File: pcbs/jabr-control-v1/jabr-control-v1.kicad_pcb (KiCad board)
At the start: 6 copper layers, 71 x 43 mm, 7 parts, among them J4001 MDT275E01001, J8001 MSPE-J2L0-x00, U3001 PI7C9X2G303EL, U5001 LAN7431_YXX, U6001 LAN8870, U7001 STM32H533CEUx

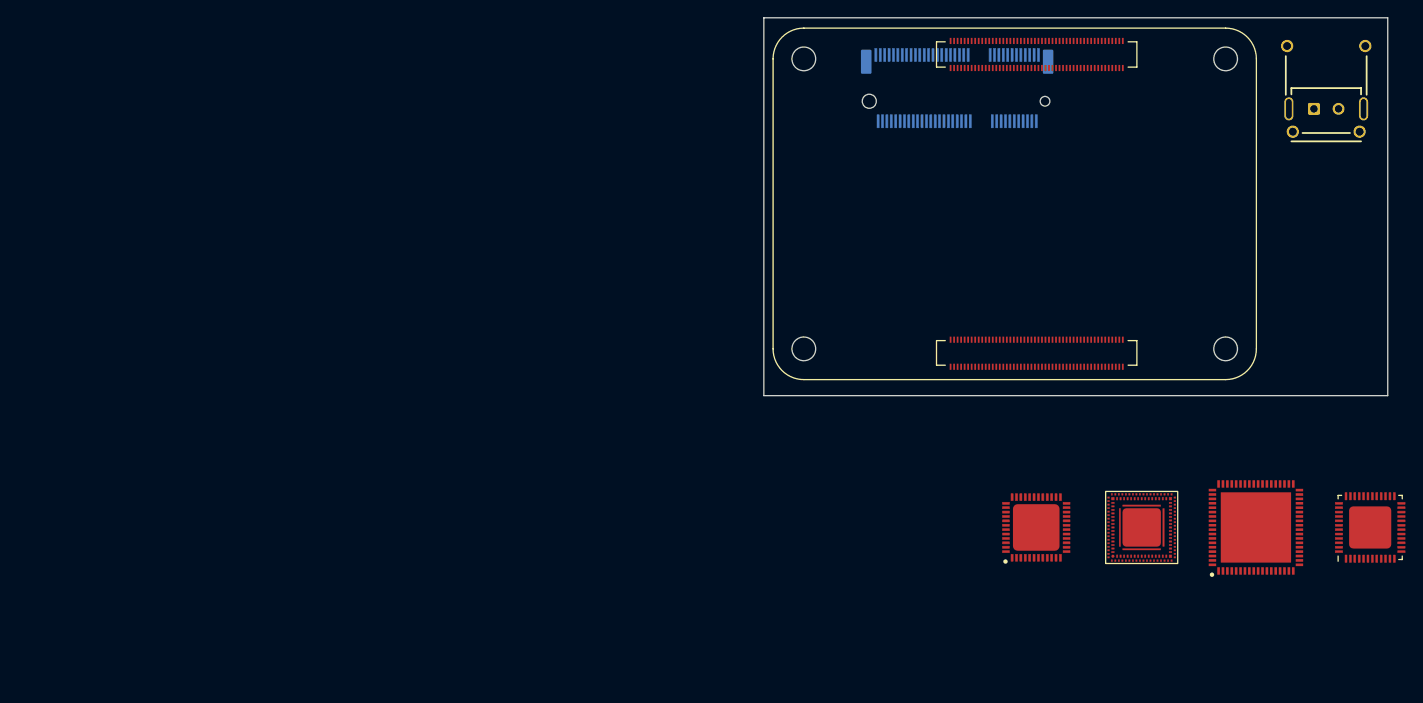
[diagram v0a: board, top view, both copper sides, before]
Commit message: Added PCIe connections
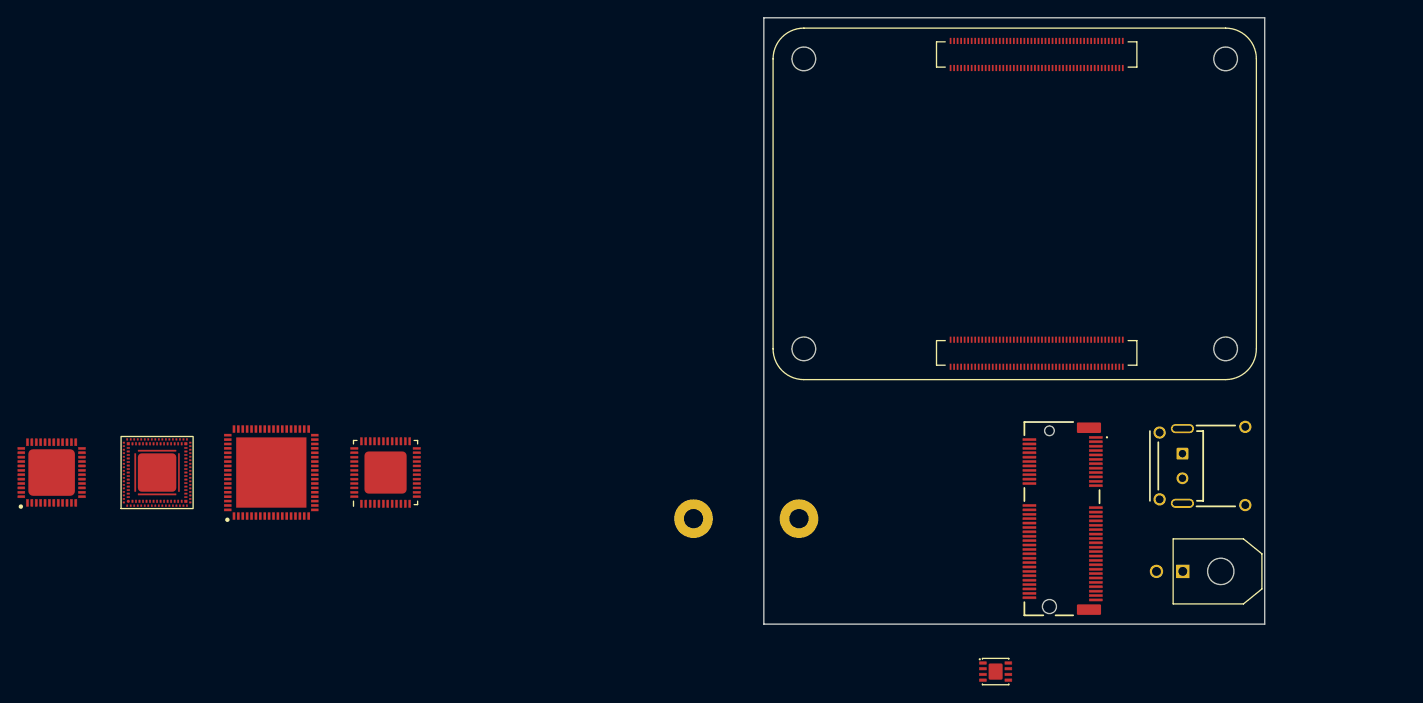
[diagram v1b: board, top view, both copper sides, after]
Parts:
- added H4001: MountingHole_Pad, MountingHole:MountingHole_2.2mm_M2_Pad, F.Cu at (125.0, 134.0)
- added H4002: MountingHole_Pad, MountingHole:MountingHole_2.2mm_M2_Pad, F.Cu at (113.0, 134.0)
- added J9001: 43045-0201, project_footprints:43045-02YY, F.Cu at (168.7, 140.0)
- added U9001: TVS3301DRBR, project_footprints:SON65P300X300X100-9N-D, F.Cu at (147.4, 151.4)
- J4001: moved to F.Cu
- moved U3001 112.2 mm to (52.0, 128.8)
- moved U5001 112.2 mm to (65.0, 128.8)
- moved U6001 112.2 mm to (78.0, 128.8)
- moved U7001 112.2 mm to (40.0, 128.8)
- moved J4001 50.4 mm to (155.0, 134.0), turned to -90 degrees
- moved J8001 43.8 mm to (168.6, 128.0), turned to 90 degrees
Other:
- board size 71 x 43 mm -> 57 x 69 mm

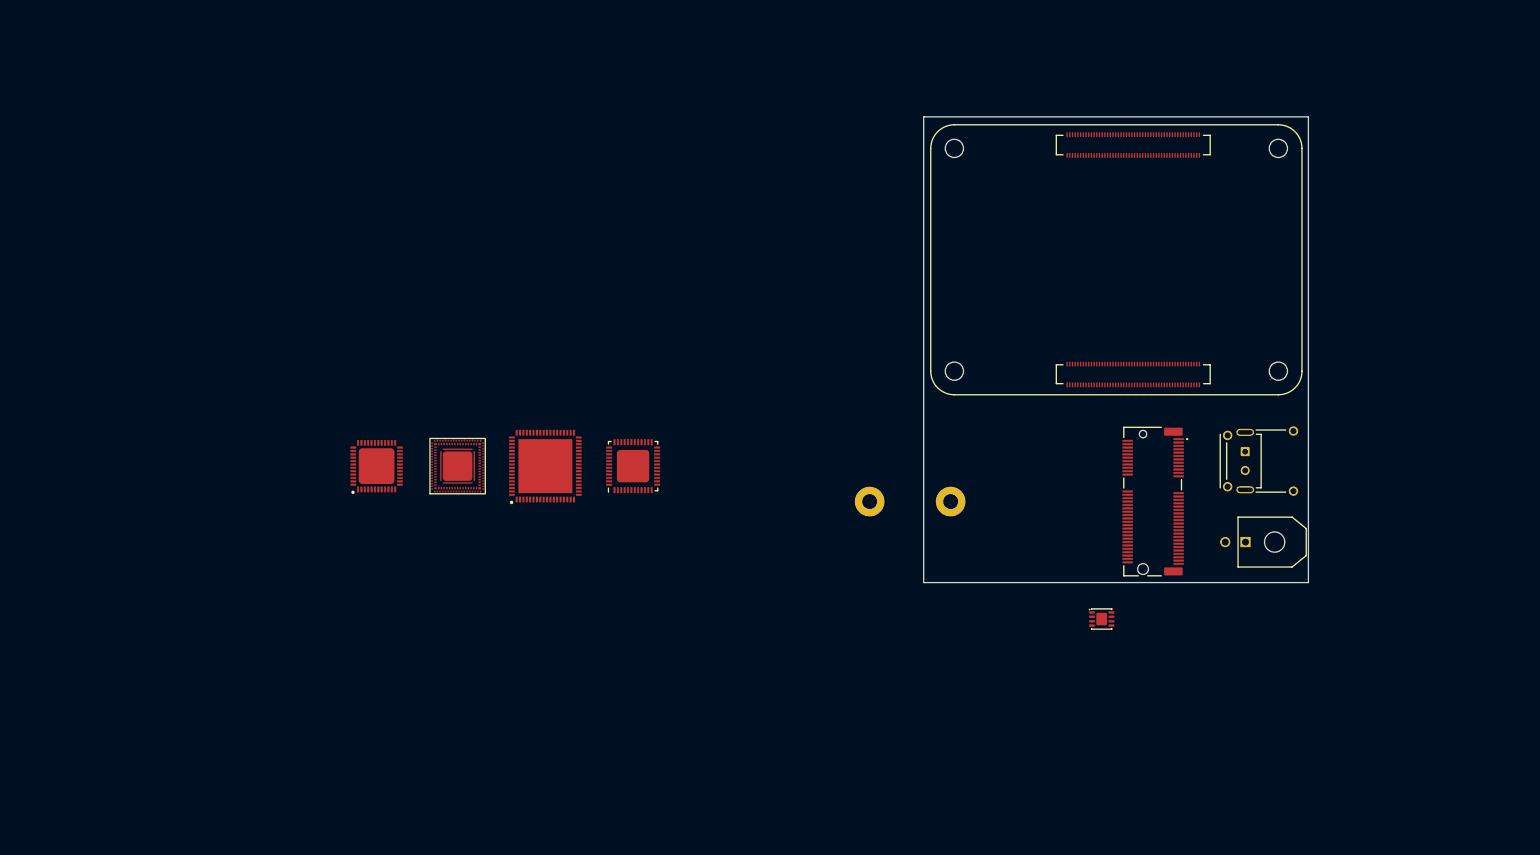
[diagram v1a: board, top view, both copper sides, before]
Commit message: Added power sheets
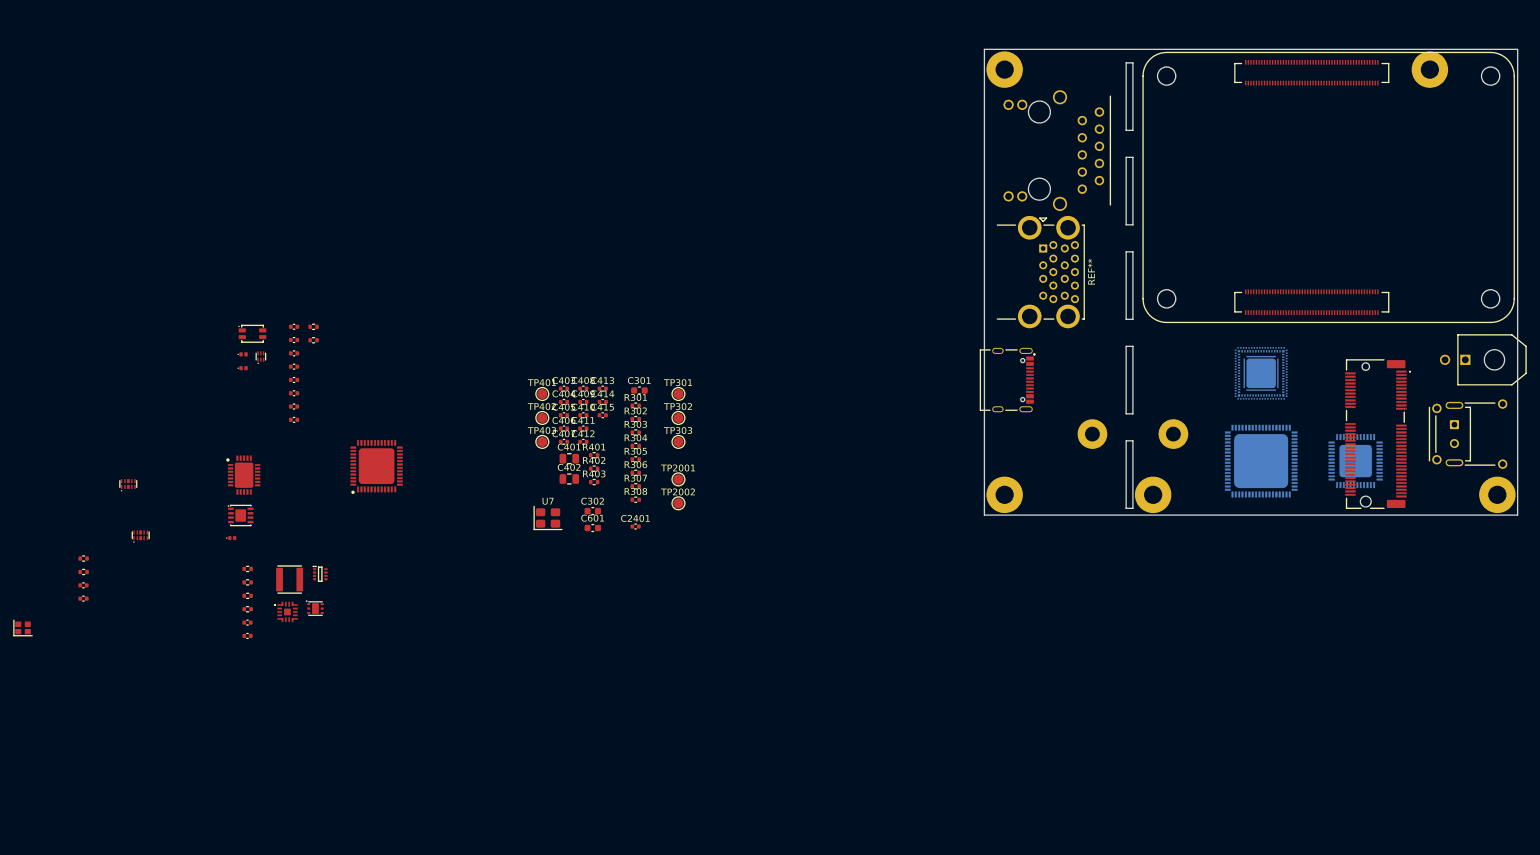
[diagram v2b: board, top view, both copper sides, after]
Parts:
- removed J8001: MSPE-J2L0-x00, project_footprints:MSPEJ2L0x00
- removed U6001: LAN8870, project_footprints:lan8870
- removed U9001: TVS3301DRBR, project_footprints:SON65P300X300X100-9N-D
- added C2401: 100n, Capacitor_SMD:C_0402_1005Metric, F.Cu at (78.3, 137.7)
- added C2935: 10p, project_footprints:C_0402, F.Cu at (-3.48, 146.4)
- added C2936: 10p, project_footprints:C_0402, F.Cu at (-3.48, 148.4)
- added C3001: 220n, project_footprints:C_0402, F.Cu at (27.7, 108.1)
- added C3002: 220n, project_footprints:C_0402, F.Cu at (27.7, 110.1)
- added C3003: 100n, project_footprints:C_0402, F.Cu at (27.7, 112.0)
- added C3004: 100n, project_footprints:C_0402, F.Cu at (27.7, 114.0)
- added C3005: 220n, project_footprints:C_0402, F.Cu at (27.7, 116.0)
- added C3006: 220n, project_footprints:C_0402, F.Cu at (27.7, 118.0)
- added C3007: 220n, project_footprints:C_0402, F.Cu at (27.7, 119.9)
- added C3008: 220n, project_footprints:C_0402, F.Cu at (27.7, 121.9)
- added C301: 100n, Capacitor_SMD:C_0603_1608Metric, F.Cu at (78.9, 117.5)
- added C302: 100n, Capacitor_SMD:C_0603_1608Metric, F.Cu at (72.0, 135.4)
- added C401: 10u, Capacitor_SMD:C_0805_2012Metric, F.Cu at (68.5, 127.6)
- added C402: 10u, Capacitor_SMD:C_0805_2012Metric, F.Cu at (68.5, 130.7)
- added C403: 1u, Capacitor_SMD:C_0402_1005Metric, F.Cu at (67.7, 117.3)
- added C404: 1u, Capacitor_SMD:C_0402_1005Metric, F.Cu at (67.7, 119.2)
- added C405: 1u, Capacitor_SMD:C_0402_1005Metric, F.Cu at (67.7, 121.2)
- added C406: 4u7, Capacitor_SMD:C_0402_1005Metric, F.Cu at (67.7, 123.2)
- added C407: 4u7, Capacitor_SMD:C_0402_1005Metric, F.Cu at (67.7, 125.2)
- added C408: 4u7, Capacitor_SMD:C_0402_1005Metric, F.Cu at (70.6, 117.3)
- added C409: 4u7, Capacitor_SMD:C_0402_1005Metric, F.Cu at (70.6, 119.2)
- added C410: 4u7, Capacitor_SMD:C_0402_1005Metric, F.Cu at (70.6, 121.2)
- added C411: 4u7, Capacitor_SMD:C_0402_1005Metric, F.Cu at (70.6, 123.2)
- added C412: 4u7, Capacitor_SMD:C_0402_1005Metric, F.Cu at (70.6, 125.2)
- added C413: 4u7, Capacitor_SMD:C_0402_1005Metric, F.Cu at (73.5, 117.3)
- added C414: 4u7, Capacitor_SMD:C_0402_1005Metric, F.Cu at (73.5, 119.2)
- added C415: 4u7, Capacitor_SMD:C_0402_1005Metric, F.Cu at (73.5, 121.2)
- added C5001: 220n, project_footprints:C_0402, F.Cu at (20.8, 151.9)
- added C5002: 220n, project_footprints:C_0402, F.Cu at (20.8, 153.9)
- added C601: 100n, Capacitor_SMD:C_0603_1608Metric, F.Cu at (72.0, 137.9)
- added D301: SZESD7241N2T5G, project_footprints:SZESD7462N2T5G, F.Cu at (18.6, 139.4)
- added D302: SZESD7241N2T5G, project_footprints:SZESD7462N2T5G, F.Cu at (20.2, 112.2)
- added D303: 824012823, project_footprints:824012823, F.Cu at (22.8, 112.5)
- added D601: SZESD7241N2T5G, project_footprints:SZESD7462N2T5G, F.Cu at (20.2, 114.2)
- added FL301: ACT1210G-800-2P-TL10, project_footprints:ACT1210G, F.Cu at (21.6, 109.1)
- added H101: M2.5, MountingHole:MountingHole_2.7mm_M2.5_Pad, F.Cu at (206.0, 133.0)
- added H102: M2.5, MountingHole:MountingHole_2.7mm_M2.5_Pad, F.Cu at (133.0, 133.0)
- added H103: M2.5, MountingHole:MountingHole_2.7mm_M2.5_Pad, F.Cu at (133.0, 70.0)
- added H104: M2.5, MountingHole:MountingHole_2.7mm_M2.5_Pad, F.Cu at (196.0, 70.0)
- added H105: M2.5, MountingHole:MountingHole_2.7mm_M2.5_Pad, F.Cu at (155.0, 133.0)
- added J10001: ARJM11D7-502-AB-EW2, project_footprints:ARJM11D7-502-AB-EW2_ABR, F.Cu at (142.0, 82.0)
- added J10002: TYPE-C-31-M-12, project_footprints:TYPE-C-31-M-12, F.Cu at (132.0, 116.0)
- added J6001: MSPE-J2L0-x00, project_footprints:MSPEJ2L0x00, F.Cu at (199.6, 124.0)
- added L401: 74479335329222, project_footprints:L_Wurth_WE-PMFI-353220, F.Cu at (27.1, 145.6)
- added R301: 120k, Resistor_SMD:R_0402_1005Metric, F.Cu at (78.3, 119.8)
- added R302: 10k, Resistor_SMD:R_0402_1005Metric, F.Cu at (78.3, 121.8)
- added R303: 4k7, Resistor_SMD:R_0402_1005Metric, F.Cu at (78.3, 123.8)
- added R304: 47k, Resistor_SMD:R_0402_1005Metric, F.Cu at (78.3, 125.8)
- added R305: 100k, Resistor_SMD:R_0402_1005Metric, F.Cu at (78.3, 127.8)
- added R306: 100k, Resistor_SMD:R_0402_1005Metric, F.Cu at (78.3, 129.7)
- added R307: 100k, Resistor_SMD:R_0402_1005Metric, F.Cu at (78.3, 131.7)
- added R308: 5k6, Resistor_SMD:R_0402_1005Metric, F.Cu at (78.3, 133.7)
- added R318: 475R, project_footprints:R_0402, F.Cu at (30.6, 108.1)
- added R319: 1k43, project_footprints:R_0402, F.Cu at (30.6, 110.1)
- added R401: 10k, Resistor_SMD:R_0402_1005Metric, F.Cu at (72.2, 127.1)
- added R402: 10k, Resistor_SMD:R_0402_1005Metric, F.Cu at (72.2, 129.1)
- added R403: 100k, Resistor_SMD:R_0402_1005Metric, F.Cu at (72.2, 131.1)
- added R5001: 200R, project_footprints:R_0402, F.Cu at (20.8, 144.0)
- added R5003: 1k5, project_footprints:R_0402, F.Cu at (20.8, 146.0)
- added R5004: 10k, project_footprints:R_0402, F.Cu at (20.8, 148.0)
- added R5005: 10k, project_footprints:R_0402, F.Cu at (20.8, 149.9)
- added R8001: 12k1, project_footprints:R_0402, F.Cu at (-3.46, 142.4)
- added R8002: 10k, project_footprints:R_0402, F.Cu at (-3.46, 144.4)
- added REF**: USB3_A_Molex_48406-0001_Horizontal_Stacked, Connector_USB:USB3_A_Molex_48406-0001_Horizontal_Stacked, F.Cu at (138.7, 96.5)
- added TP2001: 1.5mm, TestPoint:TestPoint_Pad_D1.5mm, F.Cu at (84.7, 130.7)
- added TP2002: 1.5mm, TestPoint:TestPoint_Pad_D1.5mm, F.Cu at (84.7, 134.3)
- added TP301: 1.5mm, TestPoint:TestPoint_Pad_D1.5mm, F.Cu at (84.7, 118.1)
- added TP302: 1.5mm, TestPoint:TestPoint_Pad_D1.5mm, F.Cu at (84.7, 121.6)
- added TP303: 1.5mm, TestPoint:TestPoint_Pad_D1.5mm, F.Cu at (84.7, 125.2)
- added TP401: 1.5mm, TestPoint:TestPoint_Pad_D1.5mm, F.Cu at (64.5, 118.1)
- added TP402: 1.5mm, TestPoint:TestPoint_Pad_D1.5mm, F.Cu at (64.5, 121.6)
- added TP403: 1.5mm, TestPoint:TestPoint_Pad_D1.5mm, F.Cu at (64.5, 125.2)
- added U2401: PESD4USB3BTTS-QX, project_footprints:PESD4USB3BTTSQX, F.Cu at (3.16, 131.4)
- added U2402: PESD4USB3BTTS-QX, project_footprints:PESD4USB3BTTSQX, F.Cu at (5.00, 139.0)
- added U301: TVS3301DRBR, project_footprints:SON65P300X300X100-9N-D, F.Cu at (19.8, 136.1)
- added U302: TPS26600RHFR, project_footprints:QFN50P400X500X100-25N-D, F.Cu at (20.3, 130.1)
- added U401: LMQ66430MC3RXBRQ1, project_footprints:LMQ664x0, F.Cu at (26.7, 150.3)
- added U402: TPS7B8133QDRVRQ1, project_footprints:SON65P200X200X80-7N, F.Cu at (30.9, 149.8)
- added U403: TPS2116DRL, project_footprints:SOTFL50P160X60-8N, F.Cu at (31.6, 144.8)
- added U7: ASEK-32.768KHZ-L-R-T, Crystal:Crystal_SMD_3225-4Pin_3.2x2.5mm, F.Cu at (65.3, 136.4)
- added U8001: LAN8870, project_footprints:lan8870, B.Cu at (185.0, 128.0)
- added Y8001: XRCGB25M000F3A16R0, project_footprints:XRCGB25M000F3A16R0, F.Cu at (-12.4, 152.7)
- U3001, U5001: moved to B.Cu
- moved U3001 119.8 mm to (171.0, 115.0), turned to -90 degrees
- moved U5001 106.1 mm to (171.0, 128.0), turned to 180 degrees
- moved SOM2001 46.7 mm to (157.0, 71.0), turned to -90 degrees
- moved J9001 42.3 mm to (201.2, 113.0)
- moved H4001 34.5 mm to (158.0, 124.0)
- moved H4002 34.5 mm to (146.0, 124.0)
- moved J4001 34.5 mm to (188.0, 124.0)
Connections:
- net Net-(J4001-3V3-Pad2) renamed +3V3_M2
- net Net-(SOM2001D-5V-Pad77) renamed +5V
- H4001 pad 1: unconnected-(H4001-Pad1) -> GND
- H4002 pad 1: unconnected-(H4002-Pad1) -> GND
- J4001 pad 1: Net-(J4001-GND-Pad1) -> GND
- J4001 pad 18: Net-(J4001-GND-Pad1) -> GND
- J4001 pad 3: unconnected-(J4001-USB_D+-Pad3) -> /M.2 E-Key/USB.DP
- J4001 pad 33: Net-(J4001-GND-Pad1) -> GND
- J4001 pad 35: unconnected-(J4001-PETp0-Pad35) -> /M.2 E-Key/TX_P
- J4001 pad 37: unconnected-(J4001-PETn0-Pad37) -> /M.2 E-Key/TX_N
- J4001 pad 39: Net-(J4001-GND-Pad1) -> GND
- J4001 pad 41: unconnected-(J4001-PERp0-Pad41) -> /M.2 E-Key/RX_P
- J4001 pad 43: unconnected-(J4001-PERn0-Pad43) -> /M.2 E-Key/RX_N
- J4001 pad 45: Net-(J4001-GND-Pad1) -> GND
- J4001 pad 47: unconnected-(J4001-REFCLKp0-Pad47) -> /M.2 E-Key/CLK_P
- J4001 pad 49: unconnected-(J4001-REFCLKn0-Pad49) -> /M.2 E-Key/CLK_N
- J4001 pad 5: unconnected-(J4001-USB_D--Pad5) -> /M.2 E-Key/USB.DN
- J4001 pad 51: Net-(J4001-GND-Pad1) -> GND
- J4001 pad 52: unconnected-(J4001-~{PERST0}-Pad52) -> /M.2 E-Key/~{PCIE_RST}
- J4001 pad 53: unconnected-(J4001-~{CLKREQ0}-Pad53) -> /CM5/~{PCIE_CLKREQ}
- J4001 pad 55: unconnected-(J4001-~{PEWAKE0}-Pad55) -> /CM5/~{PCIE_WAKE}
- J4001 pad 57: Net-(J4001-GND-Pad1) -> GND
- J4001 pad 63: Net-(J4001-GND-Pad1) -> GND
- J4001 pad 69: Net-(J4001-GND-Pad1) -> GND
- J4001 pad 7: Net-(J4001-GND-Pad1) -> GND
- J4001 pad 75: Net-(J4001-GND-Pad1) -> GND
- J9001 pad 1: unconnected-(J9001---Pad1) -> GND
- J9001 pad 2: unconnected-(J9001-+-Pad2) -> /Power/Power In/VIN_RAW
- SOM2001 pad 10: unconnected-(SOM2001B-ETH_0_N-Pad10) -> /CM5/ETH.TD_A_N
- SOM2001 pad 101: unconnected-(SOM2001A-USB_OTG_ID-Pad101) -> /CM5/USB_OTG_ID
- SOM2001 pad 102: unconnected-(SOM2001B-~{PCIE_CLKREQ}-Pad102) -> /CM5/~{PCIE_CLKREQ}
- SOM2001 pad 103: unconnected-(SOM2001A-USB2_N-Pad103) -> /CM5/USB.DN
- SOM2001 pad 104: unconnected-(SOM2001B-~{PCIE_WAKE}-Pad104) -> /CM5/~{PCIE_WAKE}
- SOM2001 pad 105: unconnected-(SOM2001A-USB2_P-Pad105) -> /CM5/USB.DP
- SOM2001 pad 106: unconnected-(SOM2001B-PCIE_PWR_EN-Pad106) -> /CM5/PCIE_PWR_EN
- SOM2001 pad 109: unconnected-(SOM2001B-~{PCIE_RST}-Pad109) -> /CM5/~{PCIE_RST}
- SOM2001 pad 11: unconnected-(SOM2001B-ETH_2_P-Pad11) -> /CM5/ETH.TD_C_P
- SOM2001 pad 110: unconnected-(SOM2001B-PCIE_CLK_P-Pad110) -> /CM5/CLK_P
- SOM2001 pad 111: unconnected-(SOM2001A-VBUS_EN-Pad111) -> /CM5/VBUS_EN
- SOM2001 pad 112: unconnected-(SOM2001B-PCIE_CLK_N-Pad112) -> /CM5/CLK_N
- SOM2001 pad 116: unconnected-(SOM2001B-PCIE_RX_P-Pad116) -> /CM5/RX_P
- SOM2001 pad 118: unconnected-(SOM2001B-PCIE_RX_N-Pad118) -> /CM5/RX_N
- SOM2001 pad 12: unconnected-(SOM2001B-ETH_0_P-Pad12) -> /CM5/ETH.TD_A_P
- SOM2001 pad 122: unconnected-(SOM2001B-PCIE_TX_P-Pad122) -> /CM5/TX_P
- SOM2001 pad 124: unconnected-(SOM2001B-PCIE_TX_N-Pad124) -> /CM5/TX_N
- SOM2001 pad 15: unconnected-(SOM2001B-~{ETH_LED3}-Pad15) -> /CM5/ETH_LED3
- SOM2001 pad 17: unconnected-(SOM2001B-~{ETH_LED2}-Pad17) -> /CM5/ETH_LED2
- SOM2001 pad 3: unconnected-(SOM2001B-ETH_3_P-Pad3) -> /CM5/ETH.TD_D_P
- SOM2001 pad 4: unconnected-(SOM2001B-ETH_1_P-Pad4) -> /CM5/ETH.TD_B_P
- SOM2001 pad 5: unconnected-(SOM2001B-ETH_3_N-Pad5) -> /CM5/ETH.TD_D_N
- SOM2001 pad 6: unconnected-(SOM2001B-ETH_1_N-Pad6) -> /CM5/ETH.TD_B_N
- SOM2001 pad 76: unconnected-(SOM2001D-VBAT-Pad76) -> +3V3_AON
- SOM2001 pad 9: unconnected-(SOM2001B-ETH_2_N-Pad9) -> /CM5/ETH.TD_C_N
- SOM2001 pad 92: unconnected-(SOM2001D-PWR_BUT-Pad92) -> /CM5/PWR_BUT
- SOM2001 pad 93: unconnected-(SOM2001D-~{RPIBOOT}-Pad93) -> /CM5/~{BOOT}
- SOM2001 pad 94: unconnected-(SOM2001A-CC1-Pad94) -> /CM5/USB.CC1
- SOM2001 pad 96: unconnected-(SOM2001A-CC2-Pad96) -> /CM5/USB.CC2
- SOM2001 pad 99: unconnected-(SOM2001D-PMIC_ENABLE-Pad99) -> /CM5/PMIC_EN
- U3001 pad A10: unconnected-(U3001A-PET_0_P-PadA10) -> /PCIe Switch/P0_TXP
- U3001 pad A12: unconnected-(U3001A-PET_0_N-PadA12) -> /PCIe Switch/P0_TXN
- U3001 pad A18: unconnected-(U3001C-REXT-PadA18) -> /PCIe Switch/REXT
- U3001 pad A22: unconnected-(U3001A-REFCLKN-PadA22) -> /PCIe Switch/REFCLK_0_N
- U3001 pad A24: unconnected-(U3001A-REFCLKP-PadA24) -> /PCIe Switch/REFCLK_0_P
- U3001 pad A26: unconnected-(U3001A-PER_2_N-PadA26) -> /PCIe Switch/PORT2.RX_N
- U3001 pad A28: unconnected-(U3001A-PER_2_P-PadA28) -> /PCIe Switch/PORT2.RX_P
- U3001 pad AA35: unconnected-(U3001C-CGND-PadAA35) -> GND
- U3001 pad AB37: unconnected-(U3001A-REFCLKO_2_P-PadAB37) -> /PCIe Switch/PORT2.CLK_P
- U3001 pad AD1: unconnected-(U3001B-TEST4-PadAD1) -> /PCIe Switch/TEST4
- U3001 pad AD37: unconnected-(U3001A-REFCLKO_2_N-PadAD37) -> /PCIe Switch/PORT2.CLK_N
- U3001 pad AE35: unconnected-(U3001A-REFCLKI_P-PadAE35) -> /CM5/CLK_P
- U3001 pad AF1: unconnected-(U3001B-TEST5-PadAF1) -> /PCIe Switch/TEST5
- U3001 pad AH37: unconnected-(U3001A-REFCLKI_N-PadAH37) -> /CM5/CLK_N
- U3001 pad AL35: unconnected-(U3001A-PORTSTATUS1-PadAL35) -> /PCIe Switch/PORT1_STATUS
- U3001 pad AM37: unconnected-(U3001A-PORTSTATUS2-PadAM37) -> /PCIe Switch/PORT2_STATUS
- U3001 pad AN35: unconnected-(U3001C-VDDC-PadAN35) -> Net-(U3001C-VDDC-PadAN35)
- U3001 pad AP37: unconnected-(U3001A-PORTSTATUS0-PadAP37) -> /PCIe Switch/PORT0_STATUS
- U3001 pad AR19: unconnected-(U3001C-VDDR-PadAR19) -> Net-(U3001C-VDDR-PadAR19)
- U3001 pad AR21: unconnected-(U3001B-TEST6-PadAR21) -> /PCIe Switch/TEST6
- U3001 pad AR29: unconnected-(U3001A-CLKBUF_PD-PadAR29) -> GND
- U3001 pad AR31: unconnected-(U3001C-VDDR-PadAR31) -> Net-(U3001C-VDDR-PadAR19)
- U3001 pad AU30: unconnected-(U3001C-DGND-PadAU30) -> GND
- U3001 pad AU32: unconnected-(U3001C-VDDR-PadAU32) -> Net-(U3001C-VDDR-PadAR19)
- U3001 pad B: unconnected-(U3001C-VDDC-PadB) -> Net-(U3001C-VDDC-PadAN35)
- U3001 pad C11: unconnected-(U3001A-PER_0_N-PadC11) -> /CM5/TX_N
- U3001 pad C15: unconnected-(U3001C-REXT_GND-PadC15) -> GND
- U3001 pad C19: unconnected-(U3001C-AGND-PadC19) -> GND
- U3001 pad C21: unconnected-(U3001C-AGND-PadC21) -> GND
- U3001 pad C23: unconnected-(U3001A-PET_2_N-PadC23) -> /PCIe Switch/P2_TXN
- U3001 pad C25: unconnected-(U3001A-PET_2_P-PadC25) -> /PCIe Switch/P2_TXP
- U3001 pad C27: unconnected-(U3001A-PET_1_N-PadC27) -> /PCIe Switch/P1_TXN
- U3001 pad C29: unconnected-(U3001A-PET_1_P-PadC29) -> /PCIe Switch/P1_TXP
- U3001 pad C31: unconnected-(U3001A-PER_1_N-PadC31) -> /M.2 E-Key/RX_N
- U3001 pad C33: unconnected-(U3001A-PER_1_P-PadC33) -> /M.2 E-Key/RX_P
- U3001 pad C9: unconnected-(U3001A-PER_0_P-PadC9) -> /CM5/TX_P
- U3001 pad E3: unconnected-(U3001C-VDDR-PadE3) -> Net-(U3001C-VDDR-PadAR19)
- U3001 pad E35: unconnected-(U3001C-VDDR-PadE35) -> Net-(U3001C-VDDR-PadAR19)
- U3001 pad EP: unconnected-(U3001C-VSS-PadEP) -> GND
- U3001 pad F1: unconnected-(U3001A-~{DWNRST_1}-PadF1) -> /M.2 E-Key/~{PCIE_RST}
- U3001 pad G35: unconnected-(U3001B-~{TRST}-PadG35) -> /PCIe Switch/~{TRST}
- U3001 pad H37: unconnected-(U3001B-TMS-PadH37) -> /PCIe Switch/TMS
- U3001 pad J3: unconnected-(U3001A-~{DWNRST_2}-PadJ3) -> /PCIe Switch/~{PORT2_RST}
- U3001 pad L: unconnected-(U3001C-VDDC-PadL) -> Net-(U3001C-VDDC-PadAN35)
- U3001 pad L3: unconnected-(U3001C-VDDR-PadL3) -> Net-(U3001C-VDDR-PadAR19)
- U3001 pad L35: unconnected-(U3001C-VDDC-PadL35) -> Net-(U3001C-VDDC-PadAN35)
- U3001 pad M1: unconnected-(U3001A-~{PERST}-PadM1) -> /CM5/~{PCIE_RST}
- U3001 pad M37: unconnected-(U3001C-DGND-PadM37) -> GND
- U3001 pad N3: unconnected-(U3001B-TEST1-PadN3) -> /PCIe Switch/TEST1
- U3001 pad P1: unconnected-(U3001C-VDDCAUX-PadP1) -> Net-(U3001C-VDDCAUX-PadP1)
- U3001 pad P37: unconnected-(U3001A-REFCLKO_0_P-PadP37) -> /PCIe Switch/REFCLKO_0_P
- U3001 pad R3: unconnected-(U3001C-VDDCAUX-PadR3) -> Net-(U3001C-VDDCAUX-PadP1)
- U3001 pad R35: unconnected-(U3001C-IREF-PadR35) -> /PCIe Switch/IREF
- U3001 pad T1: unconnected-(U3001B-TEST2-PadT1) -> /PCIe Switch/TEST2
- U3001 pad T37: unconnected-(U3001A-REFCLKO_0_N-PadT37) -> /PCIe Switch/REFCLKO_0_N
- U3001 pad V1: unconnected-(U3001B-TEST3-PadV1) -> /PCIe Switch/TEST3
- U3001 pad V37: unconnected-(U3001A-REFCLKO_1_P-PadV37) -> /M.2 E-Key/CLK_P
- U3001 pad W35: unconnected-(U3001C-CGND-PadW35) -> GND
- U3001 pad Y37: unconnected-(U3001A-REFCLKO_1_N-PadY37) -> /M.2 E-Key/CLK_N
- U5001 pad 1: unconnected-(U5001A-AVDDH_1-Pad1) -> Net-(U5001A-AVDDH_1)
- U5001 pad 10: unconnected-(U5001B-TX_CTL/TX_EN-Pad10) -> /PCIe to 1000BASE-T1/1000BASE-T1 PHY/TX_CTL
- U5001 pad 11: unconnected-(U5001B-TXC/TX_CLK-Pad11) -> /PCIe to 1000BASE-T1/1000BASE-T1 PHY/TX_CLK
- U5001 pad 12: unconnected-(U5001A-VDDVARIO_B_3-Pad12) -> +3V3
- U5001 pad 13: unconnected-(U5001B-RXC/RX_CLK-Pad13) -> /PCIe to 1000BASE-T1/1000BASE-T1 PHY/RX_CLK
- U5001 pad 14: unconnected-(U5001B-RX_CTL/RX_DV-Pad14) -> /PCIe to 1000BASE-T1/1000BASE-T1 PHY/RX_CTL
- U5001 pad 15: unconnected-(U5001B-RXD0-Pad15) -> /PCIe to 1000BASE-T1/1000BASE-T1 PHY/RX_D0
- U5001 pad 16: unconnected-(U5001B-RXD1-Pad16) -> /PCIe to 1000BASE-T1/1000BASE-T1 PHY/RX_D1
- U5001 pad 17: unconnected-(U5001B-RXD2-Pad17) -> /PCIe to 1000BASE-T1/1000BASE-T1 PHY/RX_D2
- U5001 pad 18: unconnected-(U5001B-RXD3-Pad18) -> /PCIe to 1000BASE-T1/1000BASE-T1 PHY/RX_D3
- U5001 pad 19: unconnected-(U5001A-VDDVARIO_B_4-Pad19) -> +3V3
- U5001 pad 2: unconnected-(U5001A-AVDDL_1-Pad2) -> Net-(U5001A-AVDD12)
- U5001 pad 20: unconnected-(U5001B-CLK125/RX_ER-Pad20) -> /PCIe to 1000BASE-T1/1000BASE-T1 PHY/CLK125
- U5001 pad 24: unconnected-(U5001A-VDD12CORE_1-Pad24) -> Net-(U5001A-AVDD12)
- U5001 pad 25: unconnected-(U5001A-VP-Pad25) -> Net-(U5001A-AVDD12)
- U5001 pad 27: unconnected-(U5001B-PCIE_RX_P-Pad27) -> /PCIe Switch/PORT2.TX_P
- U5001 pad 28: unconnected-(U5001B-PCIE_RX_N-Pad28) -> /PCIe Switch/PORT2.TX_N
- U5001 pad 3: unconnected-(U5001A-VDDVARIO_B_1-Pad3) -> +3V3
- U5001 pad 30: unconnected-(U5001B-PCIE_TX_P-Pad30) -> /PCIe to 1000BASE-T1/PCIe MAC/TXP
- U5001 pad 31: unconnected-(U5001A-VPTX-Pad31) -> Net-(U5001A-AVDD12)
- U5001 pad 32: unconnected-(U5001B-PCIE_TX_N-Pad32) -> /PCIe to 1000BASE-T1/PCIe MAC/TXN
- U5001 pad 34: unconnected-(U5001A-VPH-Pad34) -> Net-(U5001A-AVDDH_1)
- U5001 pad 35: unconnected-(U5001B-RESREF-Pad35) -> /PCIe to 1000BASE-T1/PCIe MAC/RESREF
- U5001 pad 36: unconnected-(U5001B-PCIE_CLK_P-Pad36) -> /PCIe Switch/PORT2.CLK_P
- U5001 pad 37: unconnected-(U5001B-PCIE_CLK_N-Pad37) -> /PCIe Switch/PORT2.CLK_N
- U5001 pad 4: unconnected-(U5001B-TXD3-Pad4) -> /PCIe to 1000BASE-T1/1000BASE-T1 PHY/TX_D3
- U5001 pad 40: unconnected-(U5001B-DUPLEX-Pad40) -> +3V3
- U5001 pad 41: unconnected-(U5001B-~{PHY_INT}-Pad41) -> /PCIe to 1000BASE-T1/1000BASE-T1 PHY/~{INT}
- U5001 pad 42: unconnected-(U5001B-~{PHY_RESET}-Pad42) -> /PCIe to 1000BASE-T1/1000BASE-T1 PHY/~{RST}
- U5001 pad 43: unconnected-(U5001A-VDDVARIO_1-Pad43) -> +3V3
- U5001 pad 44: unconnected-(U5001A-RESET_N-Pad44) -> /PCIe to 1000BASE-T1/~{RST}
- U5001 pad 45: unconnected-(U5001A-TEST-Pad45) -> GND
- U5001 pad 46: unconnected-(U5001A-VDD12CORE_2-Pad46) -> Net-(U5001A-AVDD12)
- U5001 pad 48: unconnected-(U5001A-VDDVARIO_2-Pad48) -> +3V3
- U5001 pad 5: unconnected-(U5001B-TXD2-Pad5) -> /PCIe to 1000BASE-T1/1000BASE-T1 PHY/TX_D2
- U5001 pad 57: unconnected-(U5001B-VAUX_DET/GPIO3-Pad57) -> /PCIe to 1000BASE-T1/PCIe MAC/VAUX_DET
- U5001 pad 6: unconnected-(U5001B-TXD1-Pad6) -> /PCIe to 1000BASE-T1/1000BASE-T1 PHY/TX_D1
- U5001 pad 61: unconnected-(U5001A-VDDVARIO_3-Pad61) -> +3V3
- U5001 pad 62: unconnected-(U5001A-VDD12CORE_3-Pad62) -> Net-(U5001A-AVDD12)
- U5001 pad 63: unconnected-(U5001B-MDIO-Pad63) -> /PCIe to 1000BASE-T1/1000BASE-T1 PHY/MDIO
- U5001 pad 64: unconnected-(U5001B-MDC-Pad64) -> /PCIe to 1000BASE-T1/1000BASE-T1 PHY/MDC
- U5001 pad 65: unconnected-(U5001A-VDD_OTP-Pad65) -> +3V3
- U5001 pad 66: unconnected-(U5001B-~{CLKREQ}-Pad66) -> /CM5/~{PCIE_CLKREQ}
- U5001 pad 67: unconnected-(U5001B-~{WAKE}-Pad67) -> /CM5/~{PCIE_WAKE}
- U5001 pad 68: unconnected-(U5001B-~{PERST}-Pad68) -> /PCIe Switch/~{PORT2_RST}
- U5001 pad 69: unconnected-(U5001A-AVDD12-Pad69) -> Net-(U5001A-AVDD12)
- U5001 pad 7: unconnected-(U5001A-VDDVARIO_B_2-Pad7) -> +3V3
- U5001 pad 72: unconnected-(U5001A-ISET-Pad72) -> /PCIe to 1000BASE-T1/PCIe MAC/ISET
- U5001 pad 8: unconnected-(U5001B-TXD0-Pad8) -> /PCIe to 1000BASE-T1/1000BASE-T1 PHY/TX_D0
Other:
- board size 57 x 69 mm -> 79 x 69 mm

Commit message: Worked on power and other areas of the schematic
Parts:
- removed C408, C409, C410, C411, C412, C413, C414, C415: 4u7, Capacitor_SMD:C_0402_1005Metric
- removed H104: M2.5, MountingHole:MountingHole_2.7mm_M2.5_Pad
- removed R305, R306, R307: 100k, Resistor_SMD:R_0402_1005Metric
- removed R308: 5k6, Resistor_SMD:R_0402_1005Metric
- removed R401: 10k, Resistor_SMD:R_0402_1005Metric
- removed REF**: USB3_A_Molex_48406-0001_Horizontal_Stacked, Connector_USB:USB3_A_Molex_48406-0001_Horizontal_Stacked
- removed TP402, TP403: 1.5mm, TestPoint:TestPoint_Pad_D1.5mm
- removed U7001: STM32H533CEUx, project_footprints:QFN50P700X700X60-49N-D
- added AE401: EMPCB.SMAFSTJ.B.HT, project_footprints:sma_edge_mount, F.Cu at (198.8, 125.0)
- added AE402: EMPCB.SMAFSTJ.B.HT, project_footprints:sma_edge_mount, F.Cu at (198.8, 138.0)
- added C1301: 22u, Capacitor_SMD:C_0805_2012Metric, F.Cu at (86.9, 170.5)
- added C1302: 4u7, Capacitor_SMD:C_0805_2012Metric, F.Cu at (86.9, 173.6)
- added C1303: 2n2, project_footprints:C_0402, F.Cu at (83.2, 170.0)
- added C1304: 100n, project_footprints:C_0402, F.Cu at (83.2, 172.0)
- added C1305: 2u2, project_footprints:C_0402, F.Cu at (83.2, 174.0)
- added C1306: 100n, project_footprints:C_0402, F.Cu at (83.2, 175.9)
- added C1307: 1n, project_footprints:C_0402, F.Cu at (83.2, 177.9)
- added C1308: 4p7, project_footprints:C_0402, F.Cu at (83.2, 179.9)
- added C1309: 22u, Capacitor_SMD:C_0805_2012Metric, F.Cu at (86.9, 176.6)
- added C1310: 22u, Capacitor_SMD:C_0805_2012Metric, F.Cu at (86.9, 179.6)
- added C1311: 22u, Capacitor_SMD:C_0805_2012Metric, F.Cu at (86.9, 182.6)
- added C1312: 2n2, project_footprints:C_0402, F.Cu at (83.2, 181.8)
- added C1313: 1u, project_footprints:C_0402, F.Cu at (83.2, 183.8)
- added C1401: 4u7, project_footprints:C_0402, F.Cu at (98.9, 170.0)
- added C1402: 4u7, project_footprints:C_0402, F.Cu at (98.9, 172.0)
- added C1403: 4u7, project_footprints:C_0402, F.Cu at (98.9, 174.0)
- added C1404: 4u7, project_footprints:C_0402, F.Cu at (98.9, 175.9)
- added C1405: 4u7, project_footprints:C_0402, F.Cu at (98.9, 177.9)
- added C1406: 4u7, project_footprints:C_0402, F.Cu at (98.9, 179.9)
- added C1407: 4u7, project_footprints:C_0402, F.Cu at (98.9, 181.8)
- added C1408: 4u7, project_footprints:C_0402, F.Cu at (98.9, 183.8)
- added C3801: 4u7, project_footprints:C_0402, F.Cu at (107.3, 170.0)
- added C3802: 4u7, project_footprints:C_0402, F.Cu at (107.3, 172.0)
- added C3804: 22p, project_footprints:C_0402, F.Cu at (107.3, 174.0)
- added C3805: 4u7, project_footprints:C_0402, F.Cu at (107.3, 175.9)
- added C3806: 4u7, project_footprints:C_0402, F.Cu at (107.3, 177.9)
- added C3807: 4u7, project_footprints:C_0402, F.Cu at (107.3, 179.9)
- added D202: PMEG4002EL-QYL, project_footprints:PMEG4002EL-QYL, F.Cu at (121.3, 170.2)
- added D2301: PMEG4002EL-QYL, project_footprints:PMEG4002EL-QYL, F.Cu at (94.0, 183.7)
- added J401: U.FL-R-SMT-K_895, project_footprints:UFLRSMTK895, F.Cu at (190.0, 128.0)
- added J402: U.FL-R-SMT-K_895, project_footprints:UFLRSMTK895, F.Cu at (190.0, 135.0)
- added L3801: 78438313015, project_footprints:L_Wurth_WE-MAIA-1610, F.Cu at (113.4, 170.8)
- added Q2602: DMN21D2UFB-7B, project_footprints:DMN21D2UFB7B, F.Cu at (94.1, 181.5)
- added R1301: 12k1, project_footprints:R_0402, F.Cu at (80.3, 170.0)
- added R1302: 100k, project_footprints:R_0402, F.Cu at (80.3, 172.0)
- added R1303: 22k, project_footprints:R_0402, F.Cu at (80.3, 174.0)
- added R1304: 10k, project_footprints:R_0402, F.Cu at (80.3, 176.0)
- added R1305: 680R, project_footprints:R_0402, F.Cu at (80.3, 178.0)
- added R1306: 12k1, project_footprints:R_0402, F.Cu at (80.3, 180.0)
- added R1307: 33k, project_footprints:R_0402, F.Cu at (80.3, 182.0)
- added R1308: 100k, project_footprints:R_0402, F.Cu at (80.3, 184.0)
- added R201: 10k, project_footprints:R_0402, F.Cu at (118.5, 170.0)
- added R203: 1k, project_footprints:R_0402, F.Cu at (118.5, 172.0)
- added R204: 1k, project_footprints:R_0402, F.Cu at (118.5, 174.0)
- added R3801: 150k, project_footprints:R_0402, F.Cu at (110.2, 170.0)
- added R3802: 180k, project_footprints:R_0402, F.Cu at (110.2, 172.0)
- added R801: 10k, project_footprints:R_0402, F.Cu at (118.5, 178.0)
- added TP1301: 1.5mm, TestPoint:TestPoint_Pad_D1.5mm, F.Cu at (90.9, 182.3)
- added TP1401: 1.5mm, TestPoint:TestPoint_Pad_D1.5mm, F.Cu at (102.1, 170.8)
- added TP3801: 1.5mm, TestPoint:TestPoint_Pad_D1.5mm, F.Cu at (110.5, 178.1)
- added U1201: TPS259472ARPWR, project_footprints:TPS259472ARPWR, F.Cu at (91.8, 177.7)
- added U1301: MAX20004AFOC/VY+T, project_footprints:MAX20004AFOC_VY+, F.Cu at (92.1, 172.1)
- added U3801: TPS62290TDRVRQ1, project_footprints:SON65P200X200X80-7N, F.Cu at (110.7, 174.7)
- R304: value 47k -> 10k
- moved H103 69.0 mm to (133.0, 139.0), turned to 90 degrees
- moved H101 66.9 mm to (195.0, 67.0), turned to 90 degrees
- moved J6001 53.4 mm to (186.0, 72.4), turned to 180 degrees
- moved H102 52.3 mm to (185.0, 139.0), turned to 90 degrees
- moved J10002 50.8 mm to (176.2, 141.0), turned to 0 degrees
- moved SOM2001 50.2 mm to (133.0, 115.0), turned to 0 degrees
- moved J9001 49.7 mm to (175.0, 70.8), turned to 180 degrees
- moved J10001 49.1 mm to (145.0, 131.0), turned to 0 degrees
- moved H105 43.9 mm to (195.0, 115.0), turned to 90 degrees
- moved U8001 41.3 mm to (190.0, 87.0), turned to 180 degrees
- moved J4001 41.0 mm to (186.0, 83.0), turned to 0 degrees
- moved H4002 40.0 mm to (186.0, 125.0), turned to 90 degrees
- moved U5001 33.0 mm to (190.0, 101.0), turned to -90 degrees
- moved H4001 30.1 mm to (186.0, 113.0), turned to 90 degrees
- moved U3001 15.2 mm to (177.0, 101.0), turned to 0 degrees
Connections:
- net /Power/3V3 Regulators/MODE renamed /Power/3V3 Regulators/3V3_M2_MODE
- net Net-(SOM2001D-1V8-Pad88) renamed +1V8
- C401 pad 1: +VIN -> +5V
- C402 pad 1: +VIN -> +5V
- C406 pad 1: +3V3 -> +3V3_M2
- C407 pad 1: +3V3 -> +3V3_M2
- L401 pad 2: +3V3 -> +3V3_M2
- R403 pad 2: +3V3 -> +3V3_M2
- SOM2001 pad 21: unconnected-(SOM2001D-~{LED_ACT}-Pad21) -> /CM5/~{LED_ACT}
- SOM2001 pad 84: Net-(SOM2001D-3V3-Pad84) -> +3V3
- SOM2001 pad 86: Net-(SOM2001D-3V3-Pad84) -> +3V3
- SOM2001 pad 95: unconnected-(SOM2001D-~{LED_PWR}-Pad95) -> /CM5/~{LED_PWR}
- SOM2001 pad 99: /CM5/PMIC_EN -> unconnected-(SOM2001D-PMIC_ENABLE-Pad99)
- U302 pad 18: /Power/Power In/EFUSE_IMON -> unconnected-(U302-IMON-Pad18)
- U401 pad 1: /Power/3V3 Regulators/EN -> /CM5/PCIE_PWR_EN
- U401 pad 11: +3V3 -> +3V3_M2
- U401 pad 16: /Power/3V3 Regulators/EN -> /CM5/PCIE_PWR_EN
- U401 pad 3: +VIN -> +5V
- U403 pad 8: /Power/3V3 Regulators/3V3_AON_ST -> unconnected-(U403-ST-Pad8)
- U5001 pad 44: /PCIe to 1000BASE-T1/~{RST} -> /CM5/~{RST}
- U8001 pad 1: unconnected-(U8001B-VBAT-Pad1) -> +3V3_AON
- U8001 pad 10: Net-(U8001B-VDDCORE-Pad10) -> +1V1
- U8001 pad 13: unconnected-(U8001B-VDD_RGMII-Pad13) -> Net-(U8001B-VDDIO)
- U8001 pad 19: Net-(U8001B-VDDCORE-Pad10) -> +1V1
- U8001 pad 20: unconnected-(U8001B-VDD_RGMII_VPH-Pad20) -> Net-(U8001B-VDDIO)
- U8001 pad 29: Net-(U8001B-VDDCORE-Pad10) -> +1V1
- U8001 pad 36: unconnected-(U8001B-VDDIO-Pad36) -> Net-(U8001B-VDDIO)
- U8001 pad 4: unconnected-(U8001A-INH-Pad4) -> /PCIe to 1000BASE-T1/INH
- U8001 pad 44: Net-(U8001B-VDDACORE-Pad44) -> +1V1
- U8001 pad 46: Net-(U8001B-VDDACORE-Pad44) -> +1V1
- U8001 pad 5: Net-(U8001B-VDDACORE-Pad44) -> +1V1
- U8001 pad 8: unconnected-(U8001B-REG_EN-Pad8) -> /PCIe to 1000BASE-T1/1000BASE-T1 PHY/REG_EN
- U8001 pad 9: unconnected-(U8001B-VDD_REG-Pad9) -> +3V3
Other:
- board size 79 x 69 mm -> 70 x 80 mm

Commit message: Updated README
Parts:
- added REF**: LQFP-128_14x14mm_P0.4mm, Package_QFP:LQFP-128_14x14mm_P0.4mm, B.Cu at (174.0, 101.0)
